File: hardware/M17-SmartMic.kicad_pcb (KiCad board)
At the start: 4 copper layers, 84.9 x 89.9 mm, 184 parts, among them IC1 LM4861M, J1 Kenwood-2.5, J10 UART, J11 Radio_Opt, J12 Speaker, J2 USB_C, J3 OLED, J4 CAT_TX, J5 Kenwood-3.5, J6 CAT_TX, J7 Radio, J8 +12V, J9 STLink, Q1 IRLML2060, Q2 BSS138, Q3 BSS138, Q4 IRLML2244, Q5 MMBT3904, SW1 Button Up, SW2 Button Down, SW3 Reset, SW4 Button Escape, SW5 Button Left, SW6 Button Enter, SW7 Button Right, SW8 Button Power, U1 MAX9814, U10 STM32F405RGTx, U11 TPS7A2033, U2 TP6841S6, U3 USBLC6-2, U6 MCP6002, U7 MCP6002, X1 12 MHz TCXO, Y1 8 MHz

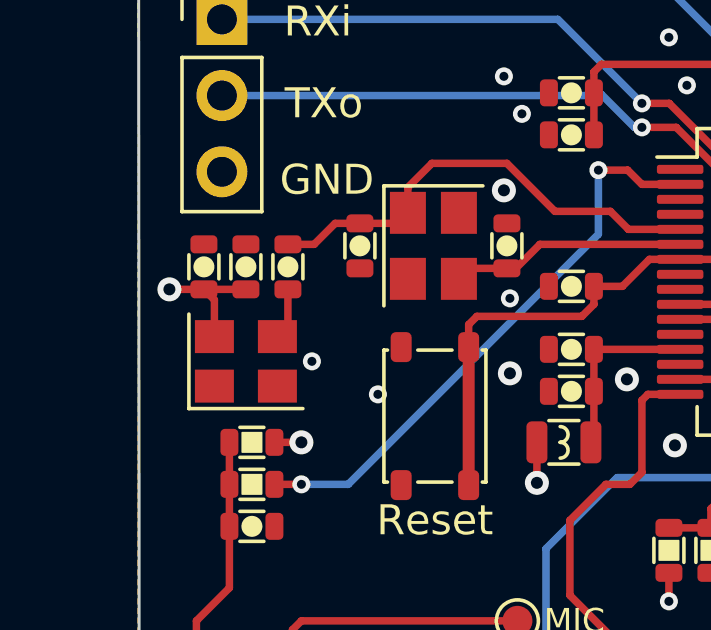
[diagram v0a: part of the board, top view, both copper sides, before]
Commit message: Removed unused TCXO
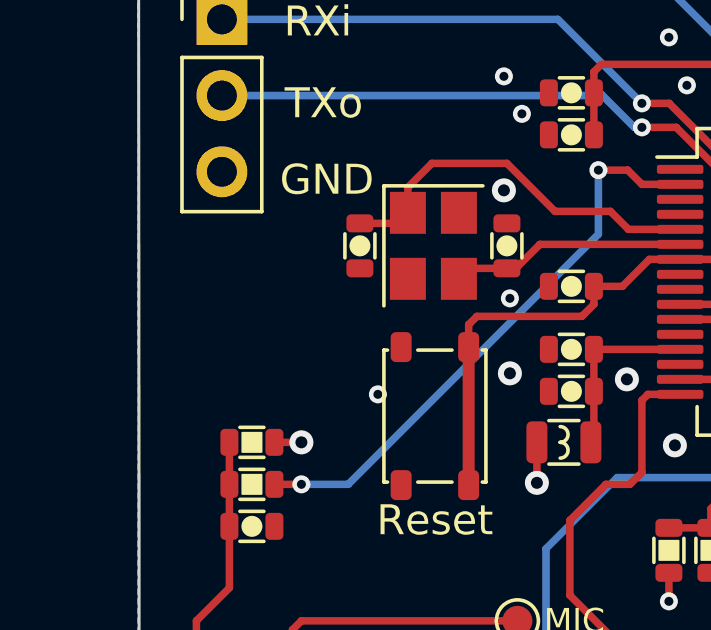
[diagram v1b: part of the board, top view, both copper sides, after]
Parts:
- removed C22, C24: 100n, pkl_dipol:C_0603
- removed C26: 4u7, pkl_dipol:C_0603
- removed X1: 12 MHz TCXO, Oscillator:Oscillator_SMD_Abracon_ASE-4Pin_3.2x2.5mm
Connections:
- net TCXO renamed Net-(U10-PH0)
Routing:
- net VDD: track 99.1 -> 94.8 mm, vias 20 -> 19
- net Net-(U10-PH0): track 15.6 -> 12.9 mm
- net Net-(X1-OUT): track 1.72 -> 0.00 mm
- net GND: vias 61 -> 60

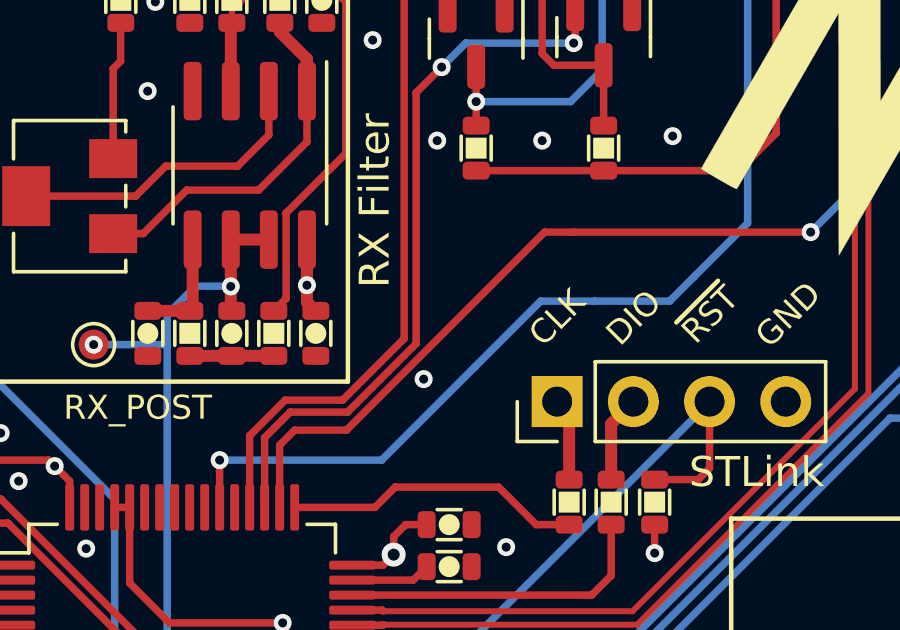
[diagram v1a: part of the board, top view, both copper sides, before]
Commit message: Added 10k pull-down
Solves the no-self-shutdown issue
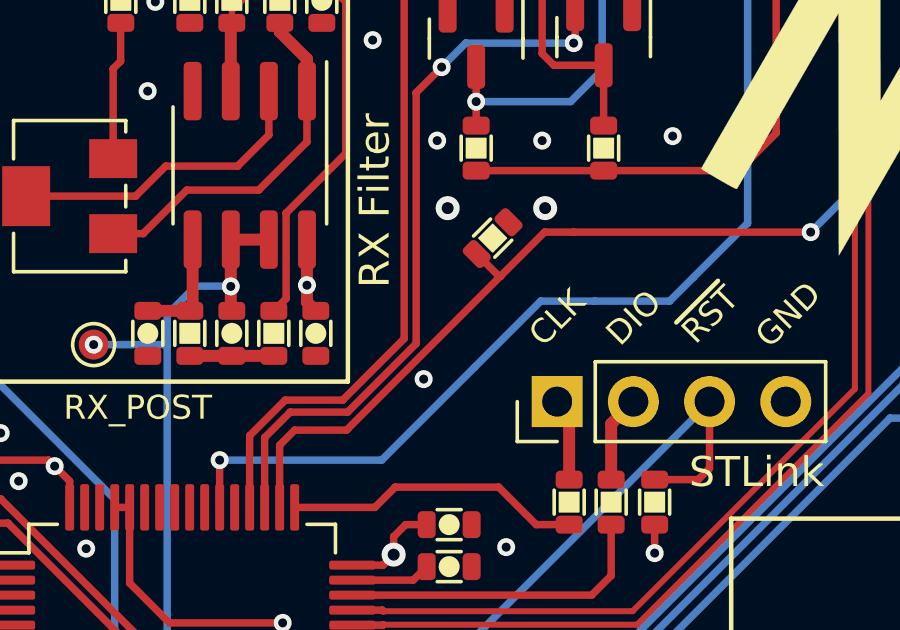
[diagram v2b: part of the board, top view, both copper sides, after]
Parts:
- added R68: 10kR, pkl_dipol:R_0603, F.Cu at (186.5, 68.0)
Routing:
- net GPIO_POWER: track 46.6 -> 47.7 mm
- net GND: vias 60 -> 62
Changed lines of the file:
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@@
     )
   )
+  (footprint "pkl_dipol:R_0603" (layer "F.Cu")
+    (at 186.5 68 45)
+    (descr "Resistor SMD 0603 (Metric 1608), reflow soldering")
+    (tags "resistor 0603")
+    (property "MPN" "Generic R/10k/0603")
+    (property "Sheetfile" "Microcontroller.kicad_sch")
+    (property "Sheetname" "Microcontroller")
+    (property "ki_description" "Resistor, small symbol")
+    (property "ki_keywords" "R resistor")
+    (attr smd)
+    (fp_text reference "R68" (at 0 -1.25 45) (layer "F.Fab")
+        (effects (font (size 0.635 0.635) (thickness 0.1)))
+    )
+    (fp_text value "10kR" (at 0 1.25 45) (layer "F.Fab")
+        (effects (font (size 0.635 0.635) (thickness 0.1)))
+    )
+    (fp_line (start -0.4 -0.5) (end 0.4 -0.5)
+      (stroke (width 0.12) (type solid)) (layer "F.SilkS"))
+    (fp_line (start 0.4 0.5) (end -0.4 0.5)
+      (stroke (width 0.12) (type solid)) (layer "F.SilkS"))
+    (fp_rect (start -0.325 -0.325) (end 0.325 0.325)
+      (stroke (width 0.05) (type solid)) (fill solid) (layer "F.SilkS"))
+    (fp_rect (start -1.25 -0.65) (end 1.25 0.65)
+      (stroke (width 0.05) (type solid)) (fill none) (layer "F.CrtYd"))
+    (fp_rect (start -0.8 -0.4) (end 0.8 0.4)
+      (stroke (width 0.1) (type solid)) (fill none) (layer "F.Fab"))
+    (pad "1" smd roundrect (at -0.75 0 45) (size 0.6 0.9) (layers "F.Cu" "F.Paste" "F.Mask") (roundrect_rratio 0.25)
+      (net 65 "GPIO_POWER") (pintype "passive"))
+    (pad "2" smd roundrect (at 0.75 0 45) (size 0.6 0.9) (layers "F.Cu" "F.Paste" "F.Mask") (roundrect_rratio 0.25)
+      (net 2 "GND") (pintype "passive"))
+    (model "${KISYS3DMOD}/Resistor_SMD.3dshapes/R_0603_1608Metric.step"
+      (offset (xyz 0 0 0))
+      (scale (xyz 1 1 1))
+      (rotate (xyz 0 0 0))
+    )
+  )
   (footprint "Capacitor_Tantalum_SMD:CP_EIA-3216-18_Kemet-A" (layer "F.Cu")
     (at 175.355 56.425 90)
@@
   (via (at 196.6 113.5) (size 0.6) (drill 0.3) (layers "F.Cu" "B.Cu") (free) (net 2))
   (via (at 235.22452 65.17548) (size 0.8) (drill 0.4) (layers "F.Cu" "B.Cu") (free) (net 2))
+  (via (at 185 67) (size 0.8) (drill 0.4) (layers "F.Cu" "B.Cu") (free) (net 2))
   (via (at 204.8 83.2) (size 0.6) (drill 0.3) (layers "F.Cu" "B.Cu") (free) (net 2))
   (via (at 165 107.5) (size 0.6) (drill 0.3) (layers "F.Cu" "B.Cu") (free) (net 2))
@@
   (via (at 209.6 41) (size 0.8) (drill 0.4) (layers "F.Cu" "B.Cu") (free) (net 2))
   (via (at 183.5 53) (size 0.6) (drill 0.3) (layers "F.Cu" "B.Cu") (free) (net 2))
+  (via (at 188.25 67) (size 0.8) (drill 0.4) (layers "F.Cu" "B.Cu") (free) (net 2))
   (via (at 168.7 85.9) (size 0.8) (drill 0.4) (layers "F.Cu" "B.Cu") (free) (net 2))
   (via (at 209.6 42.1) (size 0.8) (drill 0.4) (layers "F.Cu" "B.Cu") (free) (net 2))
@@
   (segment (start 217.9 60.55) (end 216.35 60.55) (width 0.25) (layer "F.Cu") (net 65))
   (segment (start 189.2 67.8) (end 197.1 67.8) (width 0.25) (layer "F.Cu") (net 65))
+  (segment (start 185.96967 68.53033) (end 186.704686 69.265346) (width 0.25) (layer "F.Cu") (net 65))
+  (segment (start 186.765346 69.265346) (end 188.230692 67.8) (width 0.25) (layer "F.Cu") (net 65))
   (segment (start 188.230692 67.8) (end 189.2 67.8) (width 0.25) (layer "F.Cu") (net 65))
-  (segment (start 181.630692 74.4) (end 188.230692 67.8) (width 0.25) (layer "F.Cu") (net 65))
+  (segment (start 181.630692 74.4) (end 186.765346 69.265346) (width 0.25) (layer "F.Cu") (net 65))
+  (segment (start 186.704686 69.265346) (end 186.765346 69.265346) (width 0.25) (layer "F.Cu") (net 65))
   (segment (start 179.4 76.975) (end 179.4 74.9) (width 0.25) (layer "F.Cu") (net 65))
   (segment (start 179.9 74.4) (end 181.630692 74.4) (width 0.25) (layer "F.Cu") (net 65))

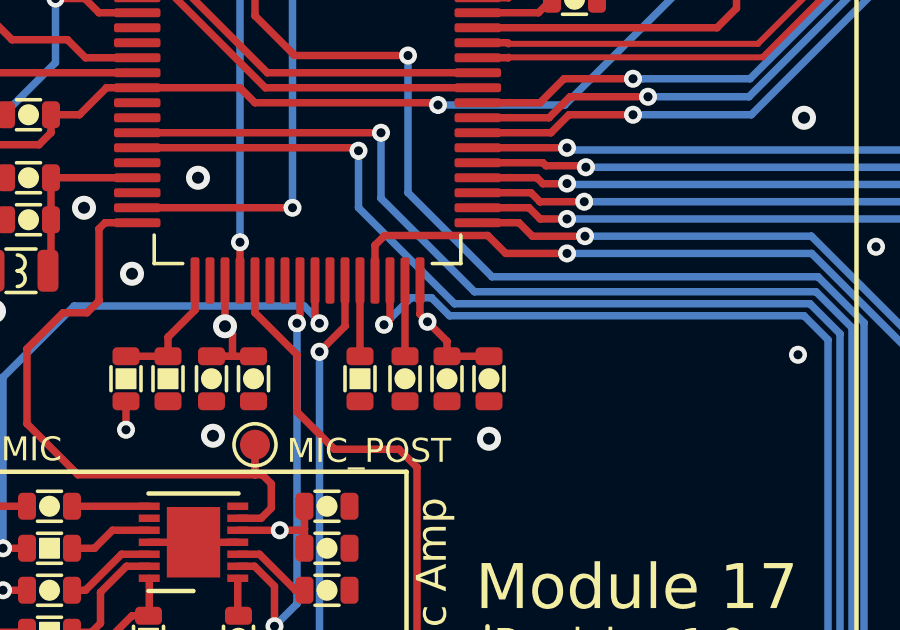
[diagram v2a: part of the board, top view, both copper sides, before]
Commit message: Set the revision detection pins to the correct voltages for Rev 1.0
PA3 set to VDD/2. PB0 set to GND.
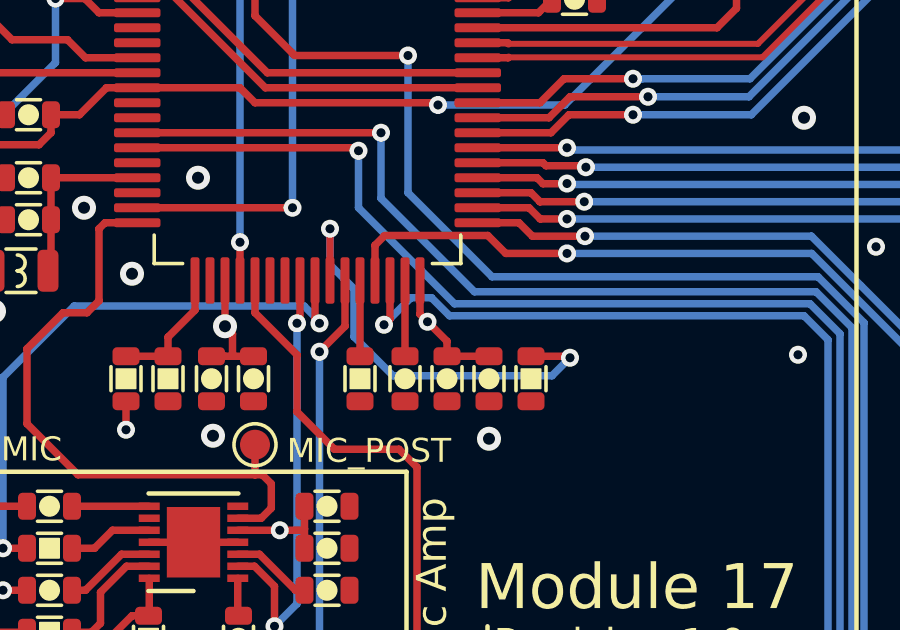
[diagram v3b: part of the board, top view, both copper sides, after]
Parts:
- added R71: 10k, pkl_dipol:R_0603, F.Cu at (183.6, 91.6)
- R53: value 0 -> 10k
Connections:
- U10 pad 26: unconnected-(U10-PB0-Pad26) -> Net-(U10-PB0)
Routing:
- net Net-(U10-PB0): track 0.00 -> 15.0 mm, vias 0 -> 2
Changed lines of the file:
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@@
   (net 137 "unconnected-(U10-PC14-Pad3)")
   (net 138 "unconnected-(U10-PC15-Pad4)")
-  (net 139 "unconnected-(U10-PB0-Pad26)")
-  (net 140 "Net-(U6A-+)")
-  (net 141 "Net-(U10-PH0)")
+  (net 139 "Net-(U6A-+)")
+  (net 140 "Net-(U10-PH0)")
+  (net 141 "Net-(U10-PB0)")
   (footprint "pkl_dipol:R_0603" (layer "F.Cu")
     (at 199.25 125.4 180)
@@
       (net 2 "GND") (pintype "passive"))
     (pad "2" smd roundrect (at 0.75 0 90) (size 0.6 0.9) (layers "F.Cu" "F.Paste" "F.Mask") (roundrect_rratio 0.25)
-      (net 141 "Net-(U10-PH0)") (pintype "passive"))
+      (net 140 "Net-(U10-PH0)") (pintype "passive"))
     (model "${KISYS3DMOD}/Capacitor_SMD.3dshapes/C_0603_1608Metric.step"
       (offset (xyz 0 0 0))
@@
   )
   (footprint "pkl_dipol:R_0603" (layer "F.Cu")
+    (at 183.6 91.6 -90)
+    (descr "Resistor SMD 0603 (Metric 1608), reflow soldering")
+    (tags "resistor 0603")
+    (property "MPN" "Generic R/10k/0603")
+    (property "Sheetfile" "Microcontroller.kicad_sch")
+    (property "Sheetname" "Microcontroller")
+    (property "ki_description" "Resistor")
+    (attr smd)
+    (fp_text reference "R71" (at 0 -1.25 90) (layer "F.Fab")
+        (effects (font (size 0.635 0.635) (thickness 0.1)))
+    )
+    (fp_text value "10k" (at 0 1.25 90) (layer "F.Fab")
+        (effects (font (size 0.635 0.635) (thickness 0.1)))
+    )
+    (fp_line (start -0.4 -0.5) (end 0.4 -0.5)
+      (stroke (width 0.12) (type solid)) (layer "F.SilkS"))
+    (fp_line (start 0.4 0.5) (end -0.4 0.5)
+      (stroke (width 0.12) (type solid)) (layer "F.SilkS"))
+    (fp_rect (start -0.325 -0.325) (end 0.325 0.325)
+      (stroke (width 0.05) (type solid)) (fill solid) (layer "F.SilkS"))
+    (fp_rect (start -1.25 -0.65) (end 1.25 0.65)
+      (stroke (width 0.05) (type solid)) (fill none) (layer "F.CrtYd"))
+    (fp_rect (start -0.8 -0.4) (end 0.8 0.4)
+      (stroke (width 0.1) (type solid)) (fill none) (layer "F.Fab"))
+    (pad "1" smd roundrect (at -0.75 0 270) (size 0.6 0.9) (layers "F.Cu" "F.Paste" "F.Mask") (roundrect_rratio 0.25)
+      (net 141 "Net-(U10-PB0)") (pintype "passive"))
+    (pad "2" smd roundrect (at 0.75 0 270) (size 0.6 0.9) (layers "F.Cu" "F.Paste" "F.Mask") (roundrect_rratio 0.25)
+      (net 2 "GND") (pintype "passive"))
+    (model "${KISYS3DMOD}/Resistor_SMD.3dshapes/R_0603_1608Metric.step"
+      (offset (xyz 0 0 0))
+      (scale (xyz 1 1 1))
+      (rotate (xyz 0 0 0))
+    )
+  )
+  (footprint "pkl_dipol:R_0603" (layer "F.Cu")
     (at 217.95 116.8 180)
     (descr "Resistor SMD 0603 (Metric 1608), reflow soldering")
@@
     (property "Sheetfile" "Microcontroller.kicad_sch")
     (property "Sheetname" "Microcontroller")
-    (property "dnp" "")
     (property "ki_description" "Resistor")
     (attr smd exclude_from_pos_files)
@@
       (net 110 "Net-(U6A--)") (pinfunction "-") (pintype "input"))
     (pad "3" smd roundrect (at -2.475 0.635 90) (size 1.95 0.6) (layers "F.Cu" "F.Paste" "F.Mask") (roundrect_rratio 0.25)
-      (net 140 "Net-(U6A-+)") (pinfunction "+") (pintype "input"))
+      (net 139 "Net-(U6A-+)") (pinfunction "+") (pintype "input"))
     (pad "4" smd roundrect (at -2.475 1.905 90) (size 1.95 0.6) (layers "F.Cu" "F.Paste" "F.Mask") (roundrect_rratio 0.25)
       (net 2 "GND") (pinfunction "V-") (pintype "power_in"))
@@
       (net 138 "unconnected-(U10-PC15-Pad4)") (pinfunction "PC15") (pintype "bidirectional+no_connect"))
     (pad "5" smd roundrect (at -5.675 -1.75) (size 1.55 0.3) (layers "F.Cu" "F.Paste" "F.Mask") (roundrect_rratio 0.25)
-      (net 141 "Net-(U10-PH0)") (pinfunction "PH0") (pintype "input"))
+      (net 140 "Net-(U10-PH0)") (pinfunction "PH0") (pintype "input"))
     (pad "6" smd roundrect (at -5.675 -1.25) (size 1.55 0.3) (layers "F.Cu" "F.Paste" "F.Mask") (roundrect_rratio 0.25)
       (net 5 "Net-(U10-PH1)") (pinfunction "PH1") (pintype "input"))
@@
       (net 92 "MIC_GAIN") (pinfunction "PC5") (pintype "bidirectional"))
     (pad "26" smd roundrect (at 0.75 5.675) (size 0.3 1.55) (layers "F.Cu" "F.Paste" "F.Mask") (roundrect_rratio 0.25)
-      (net 139 "unconnected-(U10-PB0-Pad26)") (pinfunction "PB0") (pintype "bidirectional+no_connect"))
+      (net 141 "Net-(U10-PB0)") (pinfunction "PB0") (pintype "bidirectional"))
     (pad "27" smd roundrect (at 1.25 5.675) (size 0.3 1.55) (layers "F.Cu" "F.Paste" "F.Mask") (roundrect_rratio 0.25)
       (net 80 "SPK_MUTE") (pinfunction "PB1") (pintype "bidirectional"))
@@
       (net 2 "GND") (pinfunction "1") (pintype "passive"))
     (pad "2" smd rect (at 0 1.45 90) (size 2 1.6) (layers "F.Cu" "F.Paste" "F.Mask")
-      (net 140 "Net-(U6A-+)") (pinfunction "2") (pintype "passive"))
+      (net 139 "Net-(U6A-+)") (pinfunction "2") (pintype "passive"))
     (pad "3" smd rect (at -1.25 -1.45 90) (size 1.3 1.6) (layers "F.Cu" "F.Paste" "F.Mask")
       (net 76 "BASEBAND_TX") (pinfunction "3") (pintype "passive"))
@@
       (stroke (width 0.1) (type solid)) (layer "F.Fab"))
     (pad "1" smd rect (at -1.1 0.85 270) (size 1.4 1.2) (layers "F.Cu" "F.Paste" "F.Mask")
-      (net 141 "Net-(U10-PH0)") (pinfunction "1") (pintype "passive"))
+      (net 140 "Net-(U10-PH0)") (pinfunction "1") (pintype "passive"))
     (pad "2" smd rect (at 1.1 0.85 270) (size 1.4 1.2) (layers "F.Cu" "F.Paste" "F.Mask")
       (net 2 "GND") (pinfunction "2") (pintype "passive"))
@@
     (descr "Resistor SMD 0603 (Metric 1608), reflow soldering")
     (tags "resistor 0603")
-    (property "MPN" "Generic R/2k7/0603")
+    (property "MPN" "Generic R/10k/0603")
     (property "Sheetfile" "Microcontroller.kicad_sch")
     (property "Sheetname" "Microcontroller")
@@
         (effects (font (size 0.635 0.635) (thickness 0.1)))
     )
-    (fp_text value "0" (at 0 1.25 90) (layer "F.Fab")
+    (fp_text value "10k" (at 0 1.25 90) (layer "F.Fab")
         (effects (font (size 0.635 0.635) (thickness 0.1)))
     )
@@
   (segment (start 224.98 69.45) (end 217.02 69.45) (width 0.4) (layer "F.Cu") (net 136))
   (segment (start 215.1 69.45) (end 217.02 69.45) (width 0.4) (layer "F.Cu") (net 136))
-  (segment (start 166.94 64.1356) (end 166.4596 63.6552) (width 0.4) (layer "F.Cu") (net 140))
-  (segment (start 166.4596 63.6552) (end 162.3 63.6552) (width 0.4) (layer "F.Cu") (net 140))
-  (segment (start 166.94 65.96) (end 166.94 64.1356) (width 0.4) (layer "F.Cu") (net 140))
-  (segment (start 166.3 80.3) (end 168.15 80.3) (width 0.25) (layer "F.Cu") (net 141))
-  (segment (start 168.15 80.3) (end 168.75 80.9) (width 0.25) (layer "F.Cu") (net 141))
-  (segment (start 164.7 78.7) (end 166.3 80.3) (width 0.25) (layer "F.Cu") (net 141))
-  (segment (start 161.05 80.7) (end 161.4 80.35) (width 0.25) (layer "F.Cu") (net 141))
-  (segment (start 168.75 80.9) (end 170.475 80.9) (width 0.25) (layer "F.Cu") (net 141))
-  (segment (start 162.2 78.7) (end 164.7 78.7) (width 0.25) (layer "F.Cu") (net 141))
-  (segment (start 161.4 79.5) (end 162.2 78.7) (width 0.25) (layer "F.Cu") (net 141))
-  (segment (start 159.8 80.7) (end 161.05 80.7) (width 0.25) (layer "F.Cu") (net 141))
-  (segment (start 161.4 80.35) (end 161.4 79.5) (width 0.25) (layer "F.Cu") (net 141))
+  (segment (start 166.94 64.1356) (end 166.4596 63.6552) (width 0.4) (layer "F.Cu") (net 139))
+  (segment (start 166.4596 63.6552) (end 162.3 63.6552) (width 0.4) (layer "F.Cu") (net 139))
+  (segment (start 166.94 65.96) (end 166.94 64.1356) (width 0.4) (layer "F.Cu") (net 139))
+  (segment (start 166.3 80.3) (end 168.15 80.3) (width 0.25) (layer "F.Cu") (net 140))
+  (segment (start 168.15 80.3) (end 168.75 80.9) (width 0.25) (layer "F.Cu") (net 140))
+  (segment (start 164.7 78.7) (end 166.3 80.3) (width 0.25) (layer "F.Cu") (net 140))
+  (segment (start 161.05 80.7) (end 161.4 80.35) (width 0.25) (layer "F.Cu") (net 140))
+  (segment (start 168.75 80.9) (end 170.475 80.9) (width 0.25) (layer "F.Cu") (net 140))
+  (segment (start 162.2 78.7) (end 164.7 78.7) (width 0.25) (layer "F.Cu") (net 140))
+  (segment (start 161.4 79.5) (end 162.2 78.7) (width 0.25) (layer "F.Cu") (net 140))
+  (segment (start 159.8 80.7) (end 161.05 80.7) (width 0.25) (layer "F.Cu") (net 140))
+  (segment (start 161.4 80.35) (end 161.4 79.5) (width 0.25) (layer "F.Cu") (net 140))
+  (segment (start 176.9 88.325) (end 176.9 86.6) (width 0.25) (layer "F.Cu") (net 141))
+  (segment (start 184.85 90.85) (end 183.6 90.85) (width 0.25) (layer "F.Cu") (net 141))
+  (segment (start 184.9 90.9) (end 184.85 90.85) (width 0.25) (layer "F.Cu") (net 141))
+  (via (at 184.9 90.9) (size 0.6) (drill 0.3) (layers "F.Cu" "B.Cu") (net 141))
+  (via (at 176.9 86.6) (size 0.6) (drill 0.3) (layers "F.Cu" "B.Cu") (net 141))
+  (segment (start 184.9 90.9) (end 184.3 91.5) (width 0.25) (layer "B.Cu") (net 141))
+  (segment (start 177.7 90.2) (end 177.7 88.6) (width 0.25) (layer "B.Cu") (net 141))
+  (segment (start 179 91.5) (end 177.7 90.2) (width 0.25) (layer "B.Cu") (net 141))
+  (segment (start 176.9 87.8) (end 176.9 86.6) (width 0.25) (layer "B.Cu") (net 141))
+  (segment (start 177.7 88.6) (end 176.9 87.8) (width 0.25) (layer "B.Cu") (net 141))
+  (segment (start 184.3 91.5) (end 179 91.5) (width 0.25) (layer "B.Cu") (net 141))
   (zone (net 47) (net_name "Net-(U2-SW)") (layer "F.Cu") (hatch edge 0.508)
     (priority 3)
